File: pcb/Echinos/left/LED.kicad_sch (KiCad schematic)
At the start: 14 parts

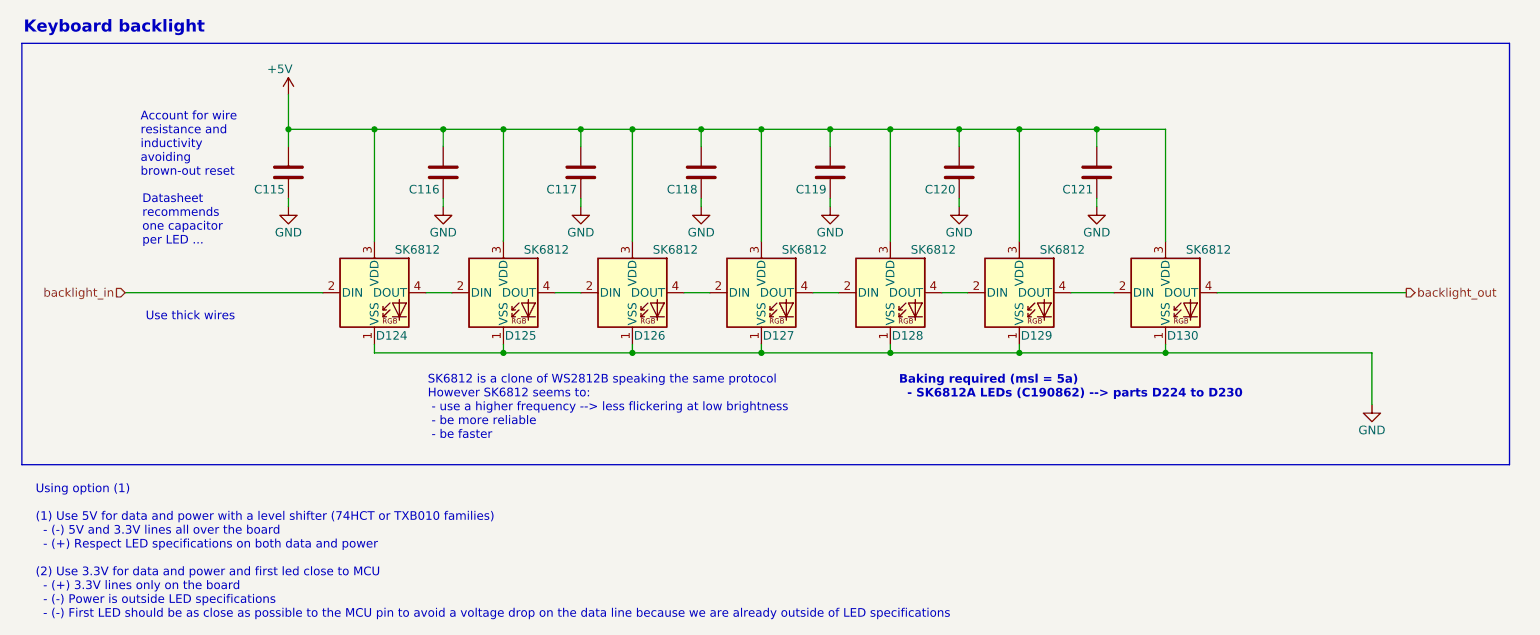
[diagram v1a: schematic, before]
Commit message: 💥 [PCB] - Group left and right on the same PCB.   - Schematics are different for each side   - Split trace naming to avoid mixing right and left   - Add mouse bite between both halves to make manufacturing easier (new footprint)
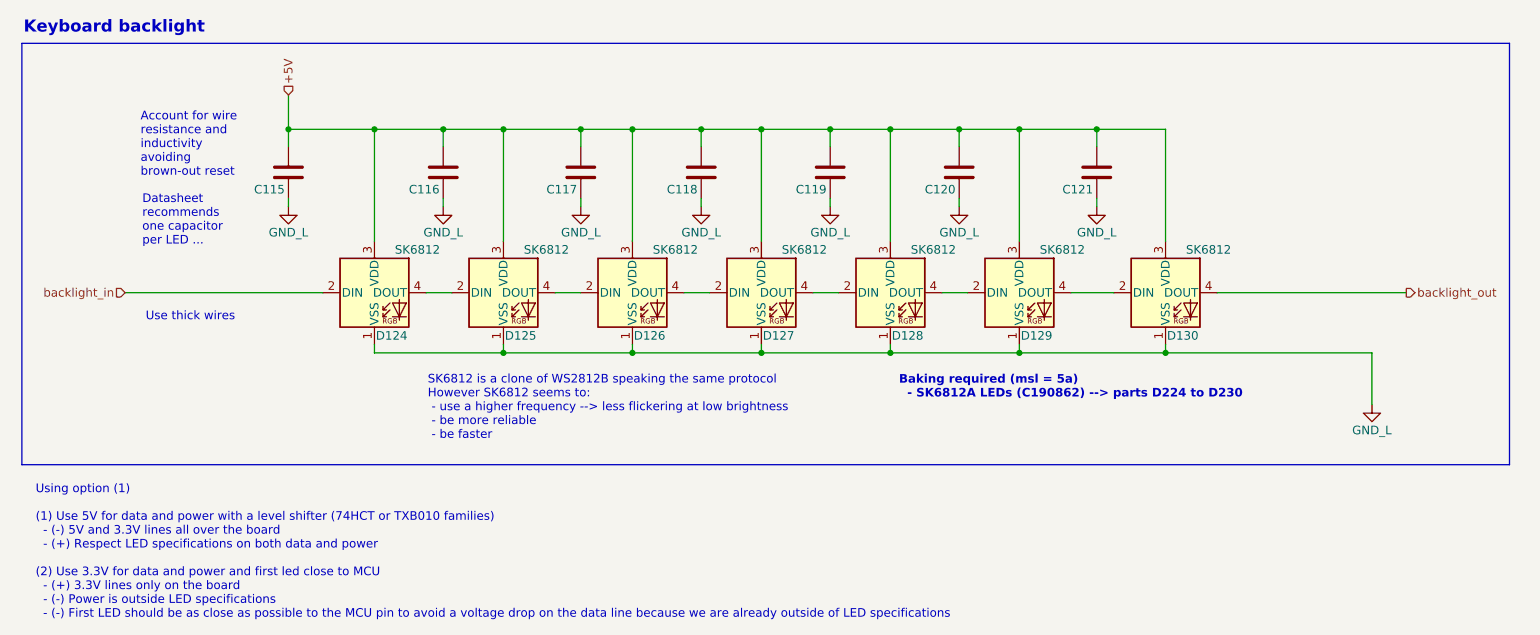
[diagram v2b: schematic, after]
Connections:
- net GND renamed GND_L
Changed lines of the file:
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@@
 		)
 	)
+	(hierarchical_label "+5V"
+		(shape input)
+		(at 58.42 26.035 90)
+		(effects
+			(font
+				(size 1.27 1.27)
+			)
+			(justify left)
+		)
+	)
 	(hierarchical_label "backlight_out"
 		(shape output)
@@
 		)
 		(instances
-			(project "Echinos_Left"
+			(project "Echinos"
 				(path "/5bd3006d-ec09-4ffb-bec3-03fa5613b46a/543aedce-e9ee-4fb5-8ab9-5c11613569bb/d7b817c5-5130-4c2e-ac26-b341cad9c61d"
 					(reference "D127")
@@
 		)
 		(instances
-			(project "Echinos_Left"
+			(project "Echinos"
 				(path "/5bd3006d-ec09-4ffb-bec3-03fa5613b46a/543aedce-e9ee-4fb5-8ab9-5c11613569bb/d7b817c5-5130-4c2e-ac26-b341cad9c61d"
 					(reference "D124")
@@
 		)
 		(instances
-			(project "Echinos_Left"
+			(project "Echinos"
 				(path "/5bd3006d-ec09-4ffb-bec3-03fa5613b46a/543aedce-e9ee-4fb5-8ab9-5c11613569bb/d7b817c5-5130-4c2e-ac26-b341cad9c61d"
 					(reference "C120")
@@
 		)
 		(instances
-			(project "Echinos_Left"
+			(project "Echinos"
 				(path "/5bd3006d-ec09-4ffb-bec3-03fa5613b46a/543aedce-e9ee-4fb5-8ab9-5c11613569bb/d7b817c5-5130-4c2e-ac26-b341cad9c61d"
 					(reference "C121")
@@
 		)
 		(instances
-			(project "Echinos_Left"
+			(project "Echinos"
 				(path "/5bd3006d-ec09-4ffb-bec3-03fa5613b46a/543aedce-e9ee-4fb5-8ab9-5c11613569bb/d7b817c5-5130-4c2e-ac26-b341cad9c61d"
 					(reference "C117")
@@
 		(in_pos_files yes)
 		(dnp no)
-		(property "Reference" "#PWR0120"
+		(property "Reference" "#PWR0121"
 			(at 177.8 48.895 0)
 			(hide yes)
@@
 			)
 		)
-		(property "Value" "GND"
+		(property "Value" "GND_L"
 			(at 177.8 46.355 0)
 			(show_name no)
@@
 		)
 		(instances
-			(project "Echinos_Left"
+			(project "Echinos"
 				(path "/5bd3006d-ec09-4ffb-bec3-03fa5613b46a/543aedce-e9ee-4fb5-8ab9-5c11613569bb/d7b817c5-5130-4c2e-ac26-b341cad9c61d"
-					(reference "#PWR0120")
+					(reference "#PWR0121")
 					(unit 1)
 				)
@@
 		(in_pos_files yes)
 		(dnp no)
-		(property "Reference" "#PWR0115"
+		(property "Reference" "#PWR0116"
 			(at 81.28 48.895 0)
 			(hide yes)
@@
 			)
 		)
-		(property "Value" "GND"
+		(property "Value" "GND_L"
 			(at 81.28 46.355 0)
 			(show_name no)
@@
 		)
 		(instances
-			(project "Echinos_Left"
+			(project "Echinos"
 				(path "/5bd3006d-ec09-4ffb-bec3-03fa5613b46a/543aedce-e9ee-4fb5-8ab9-5c11613569bb/d7b817c5-5130-4c2e-ac26-b341cad9c61d"
-					(reference "#PWR0115")
+					(reference "#PWR0116")
 					(unit 1)
 				)
@@
 		)
 		(instances
-			(project "Echinos_Left"
+			(project "Echinos"
 				(path "/5bd3006d-ec09-4ffb-bec3-03fa5613b46a/543aedce-e9ee-4fb5-8ab9-5c11613569bb/d7b817c5-5130-4c2e-ac26-b341cad9c61d"
 					(reference "D130")
@@
 	)
 	(symbol
-		(lib_id "power:+3.3V")
-		(at 58.42 26.035 0)
-		(unit 1)
-		(body_style 1)
-		(exclude_from_sim no)
-		(in_bom yes)
-		(on_board yes)
-		(in_pos_files yes)
-		(dnp no)
-		(property "Reference" "#PWR0113"
-			(at 58.42 29.845 0)
-			(hide yes)
-			(show_name no)
-			(do_not_autoplace no)
-			(effects
-				(font
-					(size 1.27 1.27)
-				)
-			)
-		)
-		(property "Value" "+5V"
-			(at 57.15 22.225 0)
-			(show_name no)
-			(do_not_autoplace no)
-			(effects
-				(font
-					(size 1.27 1.27)
-				)
-			)
-		)
-		(property "Footprint" ""
-			(at 58.42 26.035 0)
-			(hide yes)
-			(show_name no)
-			(do_not_autoplace no)
-			(effects
-				(font
-					(size 1.27 1.27)
-				)
-			)
-		)
-		(property "Datasheet" ""
-			(at 58.42 26.035 0)
-			(hide yes)
-			(show_name no)
-			(do_not_autoplace no)
-			(effects
-				(font
-					(size 1.27 1.27)
-				)
-			)
-		)
-		(property "Description" "Power symbol creates a global label with name \"+3.3V\""
-			(at 58.42 26.035 0)
-			(hide yes)
-			(show_name no)
-			(do_not_autoplace no)
-			(effects
-				(font
-					(size 1.27 1.27)
-				)
-			)
-		)
-		(pin "1"
-		)
-		(instances
-			(project "Echinos_Left"
-				(path "/5bd3006d-ec09-4ffb-bec3-03fa5613b46a/543aedce-e9ee-4fb5-8ab9-5c11613569bb/d7b817c5-5130-4c2e-ac26-b341cad9c61d"
-					(reference "#PWR0113")
-					(unit 1)
-				)
-			)
-		)
-	)
-	(symbol
 		(lib_id "power:GND")
 		(at 218.44 71.755 0)
@@
 		(in_pos_files yes)
 		(dnp no)
-		(property "Reference" "#PWR0121"
+		(property "Reference" "#PWR0122"
 			(at 218.44 78.105 0)
 			(hide yes)
@@
 			)
 		)
-		(property "Value" "GND"
+		(property "Value" "GND_L"
 			(at 218.44 75.565 0)
 			(show_name no)
@@
 		)
 		(instances
-			(project "Echinos_Left"
+			(project "Echinos"
 				(path "/5bd3006d-ec09-4ffb-bec3-03fa5613b46a/543aedce-e9ee-4fb5-8ab9-5c11613569bb/d7b817c5-5130-4c2e-ac26-b341cad9c61d"
-					(reference "#PWR0121")
+					(reference "#PWR0122")
 					(unit 1)
 				)
@@
 		)
 		(instances
-			(project "Echinos_Left"
+			(project "Echinos"
 				(path "/5bd3006d-ec09-4ffb-bec3-03fa5613b46a/543aedce-e9ee-4fb5-8ab9-5c11613569bb/d7b817c5-5130-4c2e-ac26-b341cad9c61d"
 					(reference "C115")
@@
 		)
 		(instances
-			(project "Echinos_Left"
+			(project "Echinos"
 				(path "/5bd3006d-ec09-4ffb-bec3-03fa5613b46a/543aedce-e9ee-4fb5-8ab9-5c11613569bb/d7b817c5-5130-4c2e-ac26-b341cad9c61d"
 					(reference "C116")
@@
 		)
 		(instances
-			(project "Echinos_Left"
+			(project "Echinos"
 				(path "/5bd3006d-ec09-4ffb-bec3-03fa5613b46a/543aedce-e9ee-4fb5-8ab9-5c11613569bb/d7b817c5-5130-4c2e-ac26-b341cad9c61d"
 					(reference "C119")
@@
 		)
 		(instances
-			(project "Echinos_Left"
+			(project "Echinos"
 				(path "/5bd3006d-ec09-4ffb-bec3-03fa5613b46a/543aedce-e9ee-4fb5-8ab9-5c11613569bb/d7b817c5-5130-4c2e-ac26-b341cad9c61d"
 					(reference "C118")
@@
 		)
 		(instances
-			(project "Echinos_Left"
+			(project "Echinos"
 				(path "/5bd3006d-ec09-4ffb-bec3-03fa5613b46a/543aedce-e9ee-4fb5-8ab9-5c11613569bb/d7b817c5-5130-4c2e-ac26-b341cad9c61d"
 					(reference "D128")
@@
 		(in_pos_files yes)
 		(dnp no)
-		(property "Reference" "#PWR0119"
+		(property "Reference" "#PWR0120"
 			(at 157.48 48.895 0)
 			(hide yes)
@@
 			)
 		)
-		(property "Value" "GND"
+		(property "Value" "GND_L"
 			(at 157.48 46.355 0)
 			(show_name no)
@@
 		)
 		(instances
-			(project "Echinos_Left"
+			(project "Echinos"
 				(path "/5bd3006d-ec09-4ffb-bec3-03fa5613b46a/543aedce-e9ee-4fb5-8ab9-5c11613569bb/d7b817c5-5130-4c2e-ac26-b341cad9c61d"
-					(reference "#PWR0119")
+					(reference "#PWR0120")
 					(unit 1)
 				)
@@
 		(in_pos_files yes)
 		(dnp no)
-		(property "Reference" "#PWR0116"
+		(property "Reference" "#PWR0117"
 			(at 101.6 48.895 0)
 			(hide yes)
@@
 			)
 		)
-		(property "Value" "GND"
+		(property "Value" "GND_L"
 			(at 101.6 46.355 0)
 			(show_name no)
@@
 		)
 		(instances
-			(project "Echinos_Left"
+			(project "Echinos"
 				(path "/5bd3006d-ec09-4ffb-bec3-03fa5613b46a/543aedce-e9ee-4fb5-8ab9-5c11613569bb/d7b817c5-5130-4c2e-ac26-b341cad9c61d"
-					(reference "#PWR0116")
+					(reference "#PWR0117")
 					(unit 1)
 				)
@@
 		)
 		(instances
-			(project "Echinos_Left"
+			(project "Echinos"
 				(path "/5bd3006d-ec09-4ffb-bec3-03fa5613b46a/543aedce-e9ee-4fb5-8ab9-5c11613569bb/d7b817c5-5130-4c2e-ac26-b341cad9c61d"
 					(reference "D125")
@@
 		(in_pos_files yes)
 		(dnp no)
-		(property "Reference" "#PWR0117"
+		(property "Reference" "#PWR0118"
 			(at 119.38 48.895 0)
 			(hide yes)
@@
 			)
 		)
-		(property "Value" "GND"
+		(property "Value" "GND_L"
 			(at 119.38 46.355 0)
 			(show_name no)
@@
 		)
 		(instances
-			(project "Echinos_Left"
+			(project "Echinos"
 				(path "/5bd3006d-ec09-4ffb-bec3-03fa5613b46a/543aedce-e9ee-4fb5-8ab9-5c11613569bb/d7b817c5-5130-4c2e-ac26-b341cad9c61d"
-					(reference "#PWR0117")
+					(reference "#PWR0118")
 					(unit 1)
 				)
@@
 		(in_pos_files yes)
 		(dnp no)
-		(property "Reference" "#PWR0114"
+		(property "Reference" "#PWR0115"
 			(at 58.42 48.895 0)
 			(hide yes)
@@
 			)
 		)
-		(property "Value" "GND"
+		(property "Value" "GND_L"
 			(at 58.42 46.355 0)
 			(show_name no)
@@
 		)
 		(instances
-			(project "Echinos_Left"
+			(project "Echinos"
 				(path "/5bd3006d-ec09-4ffb-bec3-03fa5613b46a/543aedce-e9ee-4fb5-8ab9-5c11613569bb/d7b817c5-5130-4c2e-ac26-b341cad9c61d"
-					(reference "#PWR0114")
+					(reference "#PWR0115")
 					(unit 1)
 				)
@@
 		)
 		(instances
-			(project "Echinos_Left"
+			(project "Echinos"
 				(path "/5bd3006d-ec09-4ffb-bec3-03fa5613b46a/543aedce-e9ee-4fb5-8ab9-5c11613569bb/d7b817c5-5130-4c2e-ac26-b341cad9c61d"
 					(reference "D126")
@@
 		)
 		(instances
-			(project "Echinos_Left"
+			(project "Echinos"
 				(path "/5bd3006d-ec09-4ffb-bec3-03fa5613b46a/543aedce-e9ee-4fb5-8ab9-5c11613569bb/d7b817c5-5130-4c2e-ac26-b341cad9c61d"
 					(reference "D129")
@@
 		(in_pos_files yes)
 		(dnp no)
-		(property "Reference" "#PWR0118"
+		(property "Reference" "#PWR0119"
 			(at 138.43 48.895 0)
 			(hide yes)
@@
 			)
 		)
-		(property "Value" "GND"
+		(property "Value" "GND_L"
 			(at 138.43 46.355 0)
 			(show_name no)
@@
 		)
 		(instances
-			(project "Echinos_Left"
+			(project "Echinos"
 				(path "/5bd3006d-ec09-4ffb-bec3-03fa5613b46a/543aedce-e9ee-4fb5-8ab9-5c11613569bb/d7b817c5-5130-4c2e-ac26-b341cad9c61d"
-					(reference "#PWR0118")
+					(reference "#PWR0119")
 					(unit 1)
 				)
